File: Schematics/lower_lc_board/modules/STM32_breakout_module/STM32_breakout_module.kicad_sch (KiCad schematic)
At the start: 55 parts, among them J2 SWD_CONN, J3 USB_C_CONN, Q4 2N7002, SW1 SW_STM_RESET, SW2 SW_STM_BOOT_MODE, U5 STM32F103CBT6, U6 W25Q128JVS, U7 ISO1044BDR, U8 CP2102N-Axx-xQFN20, Y1 X322516MMB4SI

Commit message: analog routing, start 3V3 power routing
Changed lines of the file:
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@@
 	)
 	(junction
-		(at 135.89 123.19)
+		(at 256.54 134.62)
 		(diameter 0)
 		(color 0 0 0 0)
 	)
 	(junction
-		(at 27.94 53.34)
+		(at 135.89 123.19)
 		(diameter 0)
 		(color 0 0 0 0)
 	)
 	(junction
-		(at 255.27 134.62)
+		(at 27.94 53.34)
 		(diameter 0)
 		(color 0 0 0 0)
@@
 	(wire
 		(pts
-			(xy 248.92 134.62) (xy 255.27 134.62)
+			(xy 248.92 134.62) (xy 256.54 134.62)
 		)
 		(stroke
@@
 	(wire
 		(pts
-			(xy 255.27 134.62) (xy 256.54 134.62)
-		)
-		(stroke
-			(width 0)
-			(type default)
-		)
-	)
-	(wire
-		(pts
 			(xy 44.45 158.75) (xy 54.61 158.75)
 		)
@@
 	(symbol
 		(lib_id "power:+3V3")
-		(at 255.27 134.62 0)
+		(at 256.54 134.62 0)
 		(unit 1)
 		(exclude_from_sim no)
@@
 		(dnp no)
 		(property "Reference" "#PWR0117"
-			(at 255.27 138.43 0)
+			(at 256.54 138.43 0)
 			(effects
 				(font
@@
 		)
 		(property "Value" "+3V3"
-			(at 255.016 130.81 0)
+			(at 256.286 130.81 0)
 			(effects
 				(font
@@
 		)
 		(property "Footprint" ""
-			(at 255.27 134.62 0)
+			(at 256.54 134.62 0)
 			(effects
 				(font
@@
 		)
 		(property "Datasheet" ""
-			(at 255.27 134.62 0)
+			(at 256.54 134.62 0)
 			(effects
 				(font
@@
 		)
 		(property "Description" "Power symbol creates a global label with name \"+3V3\""
-			(at 255.27 134.62 0)
+			(at 256.54 134.62 0)
 			(effects
 				(font

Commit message: adjust routing for 0603 min. footprints
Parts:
- C13, C14, C15, C16: footprint Capacitor_SMD:C_0402_1005Metric -> Capacitor_SMD:C_0603_1608Metric; JLCPCB C1525 -> (none)
- C34: footprint Capacitor_SMD:C_0402_1005Metric -> Capacitor_SMD:C_0603_1608Metric; JLCPCB C57112 -> (none)
- R10, R9: footprint Resistor_SMD:R_0402_1005Metric -> Resistor_SMD:R_0603_1608Metric; JLCPCB C25905 -> (none)
- R11: footprint Resistor_SMD:R_0402_1005Metric -> Resistor_SMD:R_0603_1608Metric; JLCPCB C25768 -> (none)
- R12: footprint Resistor_SMD:R_0402_1005Metric -> Resistor_SMD:R_0603_1608Metric; JLCPCB C25792 -> (none)
- R14, R15, R46: footprint Resistor_SMD:R_0402_1005Metric -> Resistor_SMD:R_0603_1608Metric; JLCPCB C25104 -> (none)
- R16, R21, R45, R48, R7, R8: footprint Resistor_SMD:R_0402_1005Metric -> Resistor_SMD:R_0603_1608Metric
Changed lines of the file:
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@@
 			)
 		)
-		(property "Footprint" "Resistor_SMD:R_0402_1005Metric"
+		(property "Footprint" "Resistor_SMD:R_0603_1608Metric"
 			(at 231.648 143.51 90)
 			(effects
@@
 			)
 		)
-		(property "Footprint" "Resistor_SMD:R_0402_1005Metric"
+		(property "Footprint" "Resistor_SMD:R_0603_1608Metric"
 			(at 226.06 137.922 90)
 			(effects
@@
 			)
 		)
-		(property "JLCPCB" "C25104"
+		(property "JLCPCB" ""
 			(at 226.06 139.7 0)
 			(effects
@@
 			)
 		)
-		(property "Footprint" "Resistor_SMD:R_0402_1005Metric"
+		(property "Footprint" "Resistor_SMD:R_0603_1608Metric"
 			(at 169.672 36.83 90)
 			(effects
@@
 			)
 		)
-		(property "Footprint" "Resistor_SMD:R_0402_1005Metric"
+		(property "Footprint" "Resistor_SMD:R_0603_1608Metric"
 			(at 177.292 118.11 90)
 			(effects
@@
 			)
 		)
-		(property "JLCPCB" "C25104"
+		(property "JLCPCB" ""
 			(at 179.07 118.11 0)
 			(effects
@@
 			)
 		)
-		(property "Footprint" "Capacitor_SMD:C_0402_1005Metric"
+		(property "Footprint" "Capacitor_SMD:C_0603_1608Metric"
 			(at 65.7352 160.02 0)
 			(effects
@@
 			)
 		)
-		(property "JLCPCB" "C1525"
+		(property "JLCPCB" ""
 			(at 64.77 156.21 0)
 			(effects
@@
 			)
 		)
-		(property "Footprint" "Capacitor_SMD:C_0402_1005Metric"
+		(property "Footprint" "Capacitor_SMD:C_0603_1608Metric"
 			(at 45.4152 158.75 0)
 			(effects
@@
 			)
 		)
-		(property "JLCPCB" "C1525"
+		(property "JLCPCB" ""
 			(at 44.45 154.94 0)
 			(effects
@@
 			)
 		)
-		(property "Footprint" "Capacitor_SMD:C_0402_1005Metric"
+		(property "Footprint" "Capacitor_SMD:C_0603_1608Metric"
 			(at 55.5752 158.75 0)
 			(effects
@@
 			)
 		)
-		(property "JLCPCB" "C1525"
+		(property "JLCPCB" ""
 			(at 54.61 154.94 0)
 			(effects
@@
 			)
 		)
-		(property "Footprint" "Capacitor_SMD:C_0402_1005Metric"
+		(property "Footprint" "Capacitor_SMD:C_0603_1608Metric"
 			(at 162.8648 167.64 0)
 			(effects
@@
 			)
 		)
-		(property "JLCPCB" "C57112"
+		(property "JLCPCB" ""
 			(at 163.83 171.45 0)
 			(effects
@@
 			)
 		)
-		(property "Footprint" "Capacitor_SMD:C_0402_1005Metric"
+		(property "Footprint" "Capacitor_SMD:C_0603_1608Metric"
 			(at 35.2552 158.75 0)
 			(effects
@@
 			)
 		)
-		(property "JLCPCB" "C1525"
+		(property "JLCPCB" ""
 			(at 34.29 154.94 0)
 			(effects
@@
 			)
 		)
-		(property "Footprint" "Resistor_SMD:R_0402_1005Metric"
+		(property "Footprint" "Resistor_SMD:R_0603_1608Metric"
 			(at 217.678 63.5 90)
 			(effects
@@
 			)
 		)
-		(property "JLCPCB" "C25792"
+		(property "JLCPCB" ""
 			(at 215.9 63.5 0)
 			(effects
@@
 			)
 		)
-		(property "Footprint" "Resistor_SMD:R_0402_1005Metric"
+		(property "Footprint" "Resistor_SMD:R_0603_1608Metric"
 			(at 132.08 123.698 90)
 			(effects
@@
 			)
 		)
-		(property "JLCPCB" "C25905"
+		(property "JLCPCB" ""
 			(at 132.08 121.92 0)
 			(effects
@@
 			)
 		)
-		(property "Footprint" "Resistor_SMD:R_0402_1005Metric"
+		(property "Footprint" "Resistor_SMD:R_0603_1608Metric"
 			(at 159.258 46.99 90)
 			(effects
@@
 			)
 		)
-		(property "Footprint" "Resistor_SMD:R_0402_1005Metric"
+		(property "Footprint" "Resistor_SMD:R_0603_1608Metric"
 			(at 132.08 126.238 90)
 			(effects
@@
 			)
 		)
-		(property "JLCPCB" "C25905"
+		(property "JLCPCB" ""
 			(at 132.08 124.46 0)
 			(effects
@@
 			)
 		)
-		(property "Footprint" "Resistor_SMD:R_0402_1005Metric"
+		(property "Footprint" "Resistor_SMD:R_0603_1608Metric"
 			(at 151.638 46.99 90)
 			(effects
@@
 			)
 		)
-		(property "Footprint" "Resistor_SMD:R_0402_1005Metric"
+		(property "Footprint" "Resistor_SMD:R_0603_1608Metric"
 			(at 186.182 128.27 90)
 			(effects
@@
 			)
 		)
-		(property "Footprint" "Resistor_SMD:R_0402_1005Metric"
+		(property "Footprint" "Resistor_SMD:R_0603_1608Metric"
 			(at 217.678 55.88 90)
 			(effects
@@
 			)
 		)
-		(property "JLCPCB" "C25768"
+		(property "JLCPCB" ""
 			(at 215.9 55.88 0)
 			(effects
@@
 			)
 		)
-		(property "Footprint" "Resistor_SMD:R_0402_1005Metric"
+		(property "Footprint" "Resistor_SMD:R_0603_1608Metric"
 			(at 158.242 118.11 90)
 			(effects
@@
 			)
 		)
-		(property "JLCPCB" "C25104"
+		(property "JLCPCB" ""
 			(at 160.02 118.11 0)
 			(effects
@@
 			)
 		)
-		(property "Footprint" "Resistor_SMD:R_0402_1005Metric"
+		(property "Footprint" "Resistor_SMD:R_0603_1608Metric"
 			(at 135.382 140.97 90)
 			(effects

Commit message: more local pours and 0402 adjustments
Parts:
- R47: footprint Resistor_SMD:R_0402_1005Metric -> Resistor_SMD:R_0603_1608Metric
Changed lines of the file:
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@@
 			)
 		)
-		(property "Footprint" "Resistor_SMD:R_0402_1005Metric"
+		(property "Footprint" "Resistor_SMD:R_0603_1608Metric"
 			(at 246.38 128.778 90)
 			(effects

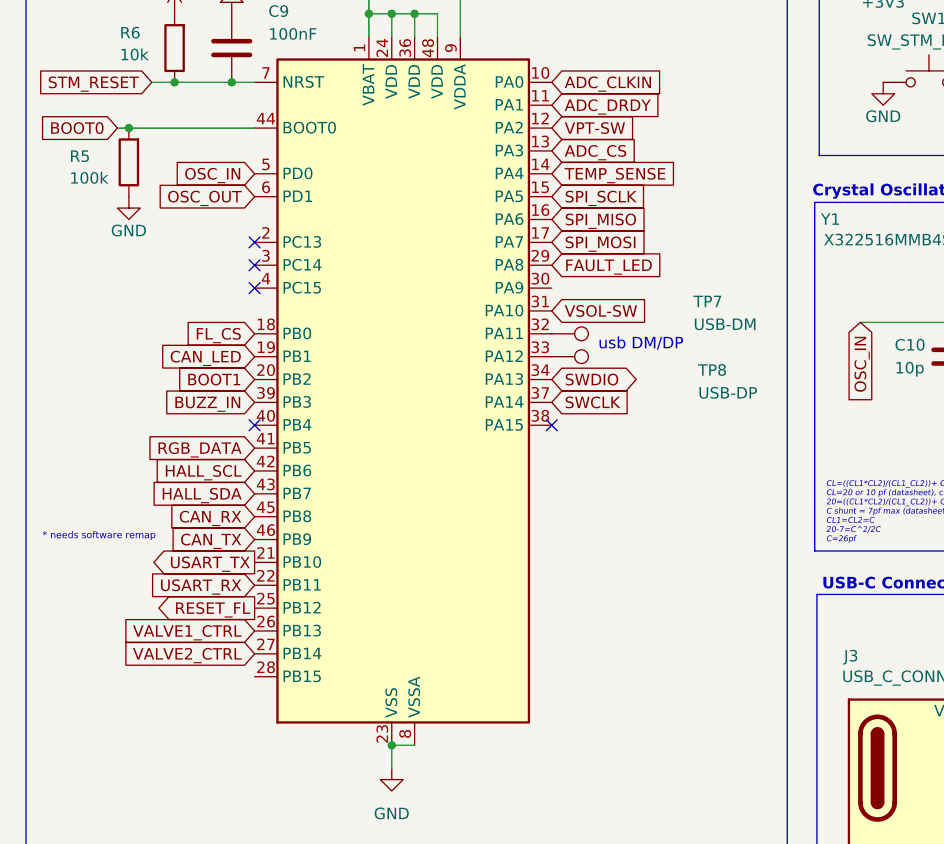
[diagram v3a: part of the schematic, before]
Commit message: review of schematics and pcb
- verified all STM pins
- reviewed all circuits
- reviewed trace clearences, made sure routes are connected, etc.
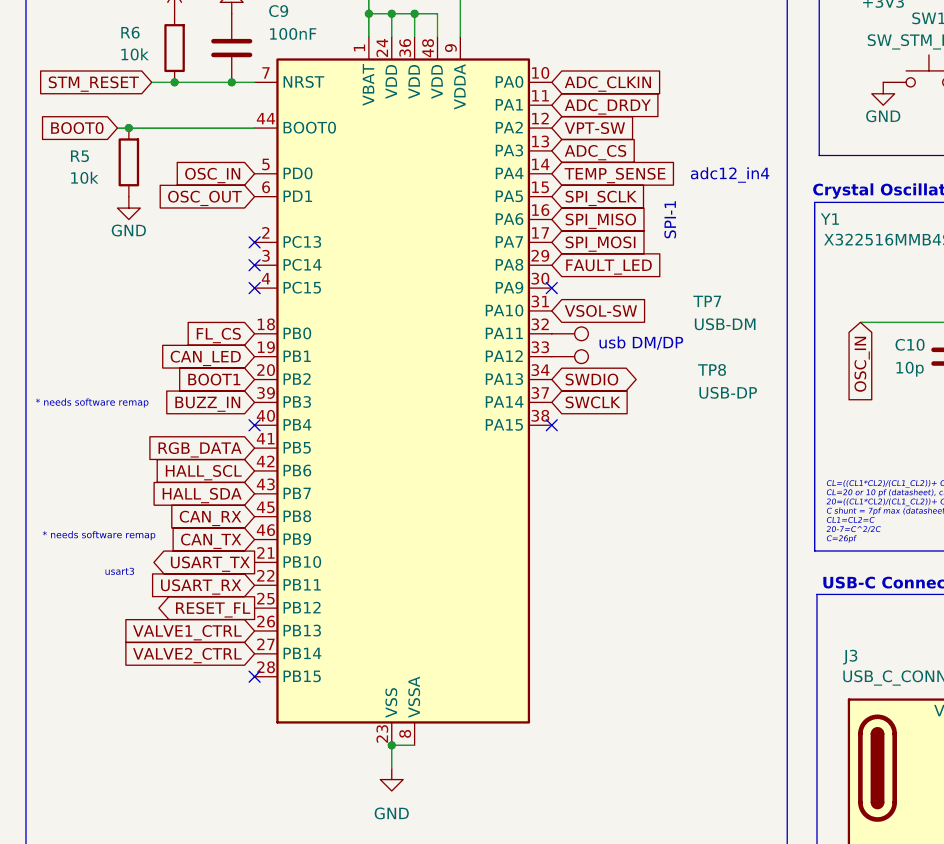
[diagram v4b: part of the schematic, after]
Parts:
- BZ1: JLCPCB (none) -> C76871
- C13, C14, C15, C16: JLCPCB (none) -> C14663
- C34: JLCPCB (none) -> C57112
- D5: LCSC C2290 -> C2286
- D8: JLCPCB (none) -> BAV16WS
- Q4: JLCPCB (none) -> C8545
- R10, R9: JLCPCB (none) -> C23186
- R11: JLCPCB (none) -> C31850
- R12: JLCPCB (none) -> C25819
- R13: footprint Capacitor_SMD:C_0402_1005Metric -> Resistor_SMD:R_0603_1608Metric; JLCPCB C11702 -> C21190
- R14: JLCPCB (none) -> C22962; LCSC C22808 -> C22962
- R15: JLCPCB (none) -> C22808
- R16: JLCPCB (none) -> C23179
- R21: JLCPCB (none) -> C25804
- R45: JLCPCB (none) -> C22843
- R46: JLCPCB (none) -> C22962
- R48, R7, R8: JLCPCB C25744 -> C25804
- R5: value 100k -> 10k; JLCPCB C25803 -> C25804
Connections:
- no-connect marks 17 -> 19
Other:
- note added: "SPI-1"
- note added: "adc12_in4"
- note added: "usart3"
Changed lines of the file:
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@@
 	)
 	(no_connect
+		(at 41.91 114.3)
+	)
+	(no_connect
+		(at 74.93 71.12)
+	)
+	(no_connect
 		(at 260.35 52.07)
 	)
@@
 		)
 	)
+	(text "usart3\n"
+		(exclude_from_sim no)
+		(at 26.924 102.87 0)
+		(effects
+			(font
+				(size 0.762 0.762)
+				(color 0 0 0 1)
+			)
+		)
+	)
 	(text "100nF \"high-quality ceramic\" for VDD and VBAT\n10uF electrolytic for bulk. \nplace as close as possible to IC."
 		(exclude_from_sim no)
@@
 		)
 	)
+	(text "SPI-1"
+		(exclude_from_sim no)
+		(at 88.138 63.754 90)
+		(effects
+			(font
+				(size 1.27 1.27)
+				(color 0 0 0 1)
+			)
+		)
+	)
 	(text "STM32 Mode Selection\n"
 		(exclude_from_sim no)
@@
 		)
 	)
+	(text "adc12_in4"
+		(exclude_from_sim no)
+		(at 94.742 58.674 0)
+		(effects
+			(font
+				(size 1.27 1.27)
+				(color 0 0 0 1)
+			)
+		)
+	)
+	(text "* needs software remap"
+		(exclude_from_sim no)
+		(at 23.876 84.074 0)
+		(effects
+			(font
+				(size 0.762 0.762)
+				(color 0 0 0 1)
+			)
+		)
+	)
 	(text "Crystal Oscillator"
 		(exclude_from_sim no)
@@
 			)
 		)
+		(property "JLCPCB" "C25804"
+			(at 229.87 143.51 0)
+			(effects
+				(font
+					(size 1.27 1.27)
+				)
+				(hide yes)
+			)
+		)
 		(pin "2"
 		)
@@
 			)
 		)
-		(property "JLCPCB" ""
+		(property "JLCPCB" "C22962"
 			(at 226.06 139.7 0)
 			(effects
@@
 			)
 		)
-		(property "Value" "100k"
+		(property "Value" "10k"
 			(at 21.336 58.928 0)
 			(effects
@@
 			)
 		)
-		(property "JLCPCB" "C25803"
+		(property "JLCPCB" "C25804"
 			(at 27.94 57.15 0)
 			(effects
@@
 			)
 		)
-		(property "JLCPCB" "C25744"
+		(property "JLCPCB" "C25804"
 			(at 171.45 36.83 0)
 			(effects
@@
 			)
 		)
-		(property "JLCPCB" ""
+		(property "JLCPCB" "C22808"
 			(at 179.07 118.11 0)
 			(effects
@@
 			)
 		)
-		(property "JLCPCB" ""
+		(property "JLCPCB" "C14663"
 			(at 64.77 156.21 0)
 			(effects
@@
 			)
 		)
-		(property "JLCPCB" ""
+		(property "JLCPCB" "C14663"
 			(at 44.45 154.94 0)
 			(effects
@@
 			)
 		)
-		(property "JLCPCB" ""
+		(property "JLCPCB" "C14663"
 			(at 54.61 154.94 0)
 			(effects
@@
 			)
 		)
-		(property "Description" "120 Ohms @ 100 MHz 1 Power Line Ferrite Bead 1206 (3216 Metric) 6A 9mOhm"
+		(property "Description" ""
 			(at 127 167.64 0)
 			(effects
@@
 			)
 		)
-		(property "JLCPCB" ""
+		(property "JLCPCB" "C57112"
 			(at 163.83 171.45 0)
 			(effects
@@
 			)
 		)
-		(property "JLCPCB" ""
+		(property "JLCPCB" "C14663"
 			(at 34.29 154.94 0)
 			(effects
@@
 			)
 		)
-		(property "JLCPCB" ""
+		(property "JLCPCB" "C25819 "
 			(at 215.9 63.5 0)
 			(effects
@@
 			)
 		)
-		(property "JLCPCB" ""
+		(property "JLCPCB" "C23186"
 			(at 132.08 121.92 0)
 			(effects
@@
 			)
 		)
-		(property "JLCPCB" "C25744"
+		(property "JLCPCB" "C25804"
 			(at 157.48 46.99 0)
 			(effects
@@
 			)
 		)
-		(property "JLCPCB" ""
+		(property "JLCPCB" "C23186"
 			(at 132.08 124.46 0)
 			(effects
@@
 			)
 		)
-		(property "JLCPCB" "C25744"
+		(property "JLCPCB" "C25804"
 			(at 149.86 46.99 0)
 			(effects
@@
 			)
 		)
+		(property "JLCPCB" "BAV16WS"
+			(at 246.38 130.81 0)
+			(effects
+				(font
+					(size 1.27 1.27)
+				)
+				(hide yes)
+			)
+		)
 		(pin "2"
 		)
@@
 			)
 		)
+		(property "JLCPCB" "C23179"
+			(at 187.96 128.27 0)
+			(effects
+				(font
+					(size 1.27 1.27)
+				)
+				(hide yes)
+			)
+		)
 		(pin "1"
 		)
@@
 			)
 		)
-		(property "JLCPCB" ""
+		(property "JLCPCB" "C31850"
 			(at 215.9 55.88 0)
 			(effects
@@
 			)
 		)
-		(property "Footprint" "Capacitor_SMD:C_0402_1005Metric"
+		(property "Footprint" "Resistor_SMD:R_0603_1608Metric"
 			(at 231.14 45.212 90)
 			(effects
@@
 			)
 		)
-		(property "JLCPCB" "C11702"
+		(property "JLCPCB" "C21190"
 			(at 231.14 46.99 0)
 			(effects
@@
 			)
 		)
-		(property "LCSC" "C22808"
+		(property "LCSC" "C22962"
 			(at 160.02 118.11 0)
 			(effects
@@
 			)
 		)
-		(property "JLCPCB" ""
+		(property "JLCPCB" "C22962"
 			(at 160.02 118.11 0)
 			(effects
@@
 			)
 		)
-		(property "LCSC" "C2290"
+		(property "LCSC" "C2286"
 			(at 160.02 125.73 90)
 			(effects
@@
 			)
 		)
+		(property "JLCPCB" "C22843"
+			(at 137.16 140.97 0)
+			(effects
+				(font
+					(size 1.27 1.27)
+				)
+				(hide yes)
+			)
+		)
 		(pin "1"
 		)
@@
 			)
 		)
+		(property "JLCPCB" "C8545"
+			(at 236.22 139.7 0)
+			(effects
+				(font
+					(size 1.27 1.27)
+				)
+				(hide yes)
+			)
+		)
 		(pin "1"
 		)
@@
 			(at 246.38 137.16 0)
 			(effects
+				(font
+					(size 1.27 1.27)
+				)
+				(hide yes)
+			)
+		)
+		(property "JLCPCB" "C76871"
+			(at 246.38 137.16 0)
+			(effects

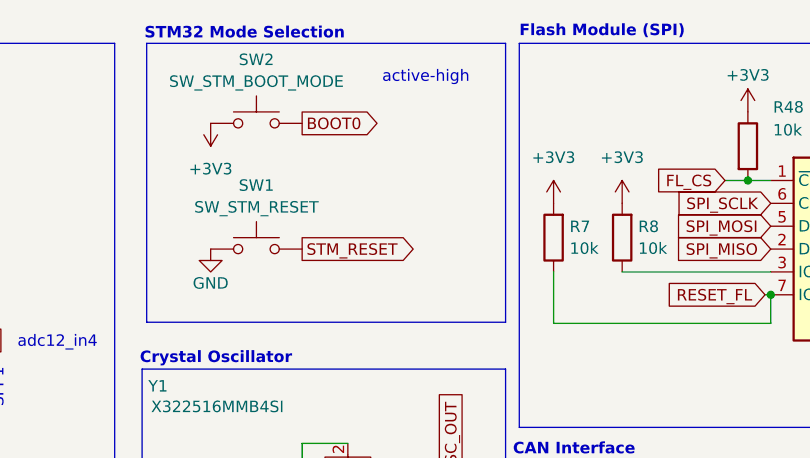
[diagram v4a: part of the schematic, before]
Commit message: WIP-commit: remove surge prot, move TH to back-side.
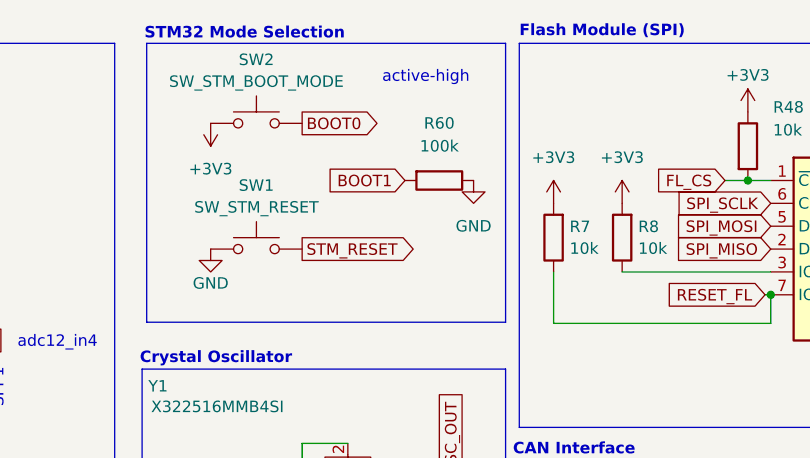
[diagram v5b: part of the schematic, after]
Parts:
- added R60: 100k, Resistor_SMD:R_0603_1608Metric, symbol Device:R
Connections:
- net BOOT1: now also R60.2
- net GND: now also R60.1
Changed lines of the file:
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@@
 		)
 	)
+	(global_label "BOOT1"
+		(shape input)
+		(at 133.35 40.64 180)
+		(fields_autoplaced yes)
+		(effects
+			(font
+				(size 1.27 1.27)
+			)
+			(justify right)
+		)
+		(property "Intersheetrefs" "${INTERSHEET_REFS}"
+			(at 124.2567 40.64 0)
+			(effects
+				(font
+					(size 1.27 1.27)
+				)
+				(justify right)
+				(hide yes)
+			)
+		)
+	)
 	(global_label "BOOT0"
 		(shape output)
@@
 	(symbol
 		(lib_id "Device:R")
+		(at 137.16 40.64 270)
+		(unit 1)
+		(exclude_from_sim no)
+		(in_bom yes)
+		(on_board yes)
+		(dnp no)
+		(fields_autoplaced yes)
+		(property "Reference" "R60"
+			(at 137.16 34.29 90)
+			(effects
+				(font
+					(size 1.27 1.27)
+				)
+			)
+		)
+		(property "Value" "100k"
+			(at 137.16 36.83 90)
+			(effects
+				(font
+					(size 1.27 1.27)
+				)
+			)
+		)
+		(property "Footprint" "Resistor_SMD:R_0603_1608Metric"
+			(at 137.16 38.862 90)
+			(effects
+				(font
+					(size 1.27 1.27)
+				)
+				(hide yes)
+			)
+		)
+		(property "Datasheet" "~"
+			(at 137.16 40.64 0)
+			(effects
+				(font
+					(size 1.27 1.27)
+				)
+				(hide yes)
+			)
+		)
+		(property "Description" ""
+			(at 137.16 40.64 0)
+			(effects
+				(font
+					(size 1.27 1.27)
+				)
+				(hide yes)
+			)
+		)
+		(property "JLCPCB" "C25804"
+			(at 137.16 40.64 0)
+			(effects
+				(font
+					(size 1.27 1.27)
+				)
+				(hide yes)
+			)
+		)
+		(pin "1"
+		)
+		(pin "2"
+		)
+		(instances
+			(project "lower_lc_board"
+				(path "/d63798c4-e363-437e-9012-e4aff32e6642/925ef91a-c900-4b94-a159-606c279d7192"
+					(reference "R60")
+					(unit 1)
+				)
+			)
+		)
+	)
+	(symbol
+		(lib_id "Device:R")
 		(at 179.07 118.11 0)
 		(unit 1)
@@
 					(unit 1)
 				)
+			)
+		)
+	)
+	(symbol
+		(lib_name "GND_4")
+		(lib_id "power:GND")
+		(at 140.97 40.64 0)
+		(unit 1)
+		(exclude_from_sim no)
+		(in_bom yes)
+		(on_board yes)
+		(dnp no)
+		(fields_autoplaced yes)
+		(property "Reference" "#PWR0108"
+			(at 140.97 46.99 0)
+			(effects
+				(font
+					(size 1.27 1.27)
+				)
+				(hide yes)
+			)
+		)
+		(property "Value" "GND"
+			(at 140.97 45.72 0)
+			(effects
+				(font
+					(size 1.27 1.27)
+				)
+			)
+		)
+		(property "Footprint" ""
+			(at 140.97 40.64 0)
+			(effects
+				(font
+					(size 1.27 1.27)
+				)
+				(hide yes)
+			)
+		)
+		(property "Datasheet" ""
+			(at 140.97 40.64 0)
+			(effects
+				(font
+					(size 1.27 1.27)
+				)
+				(hide yes)
+			)
+		)
+		(property "Description" "Power symbol creates a global label with name \"GND\" , ground"
+			(at 140.97 40.64 0)
+			(effects
+				(font
+					(size 1.27 1.27)
+				)
+				(hide yes)
+			)
+		)
+		(pin "1"
+		)
+		(instances
+			(project ""
+				(path "/d63798c4-e363-437e-9012-e4aff32e6642/925ef91a-c900-4b94-a159-606c279d7192"
+					(reference "#PWR0108")
+					(unit 1)
+				)
